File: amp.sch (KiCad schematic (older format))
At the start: 27 parts

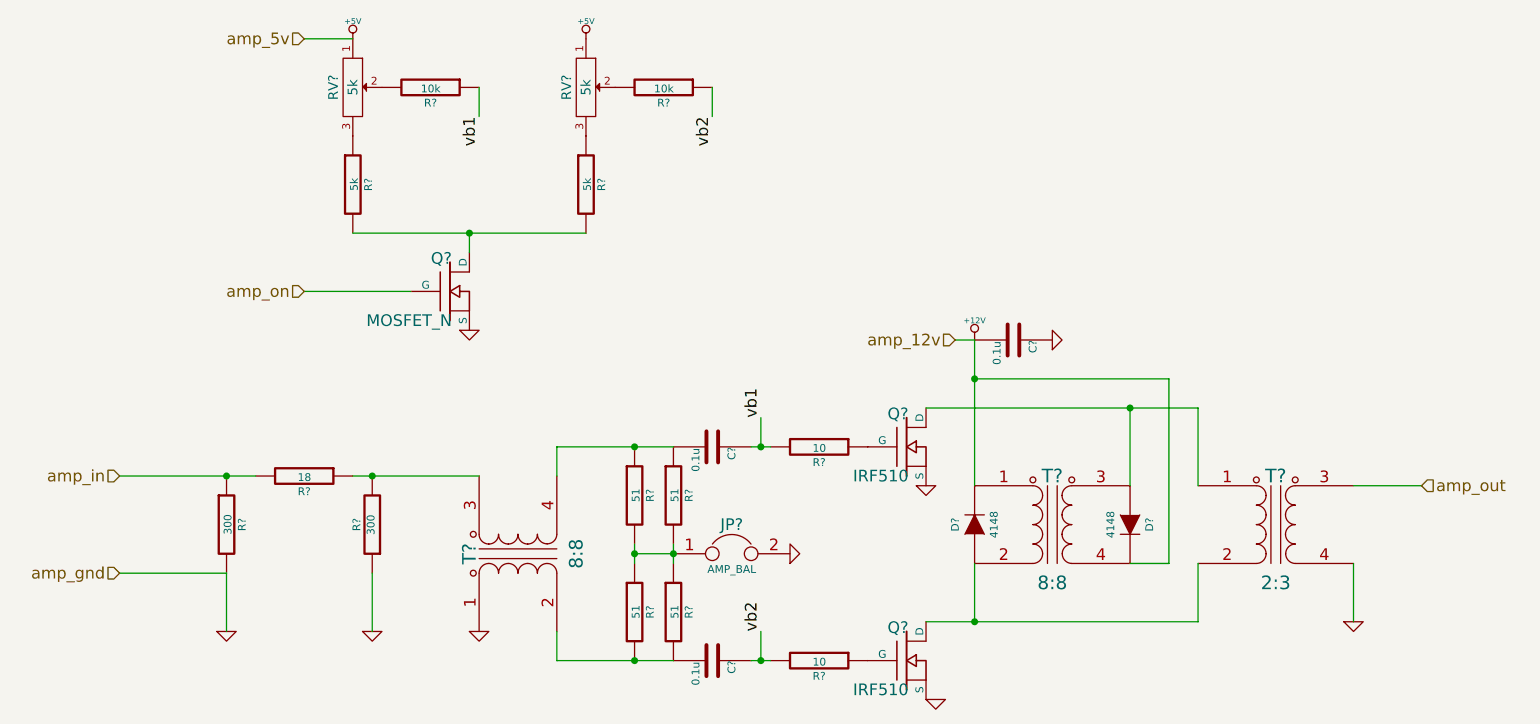
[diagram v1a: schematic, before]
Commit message: Annotated all schematics
- Added more caps to power supply
- Decided on power supply fuse part
- Changed 1n5711 SWR caps to BAT62
- Decided on MMBF170 for amp bias switch
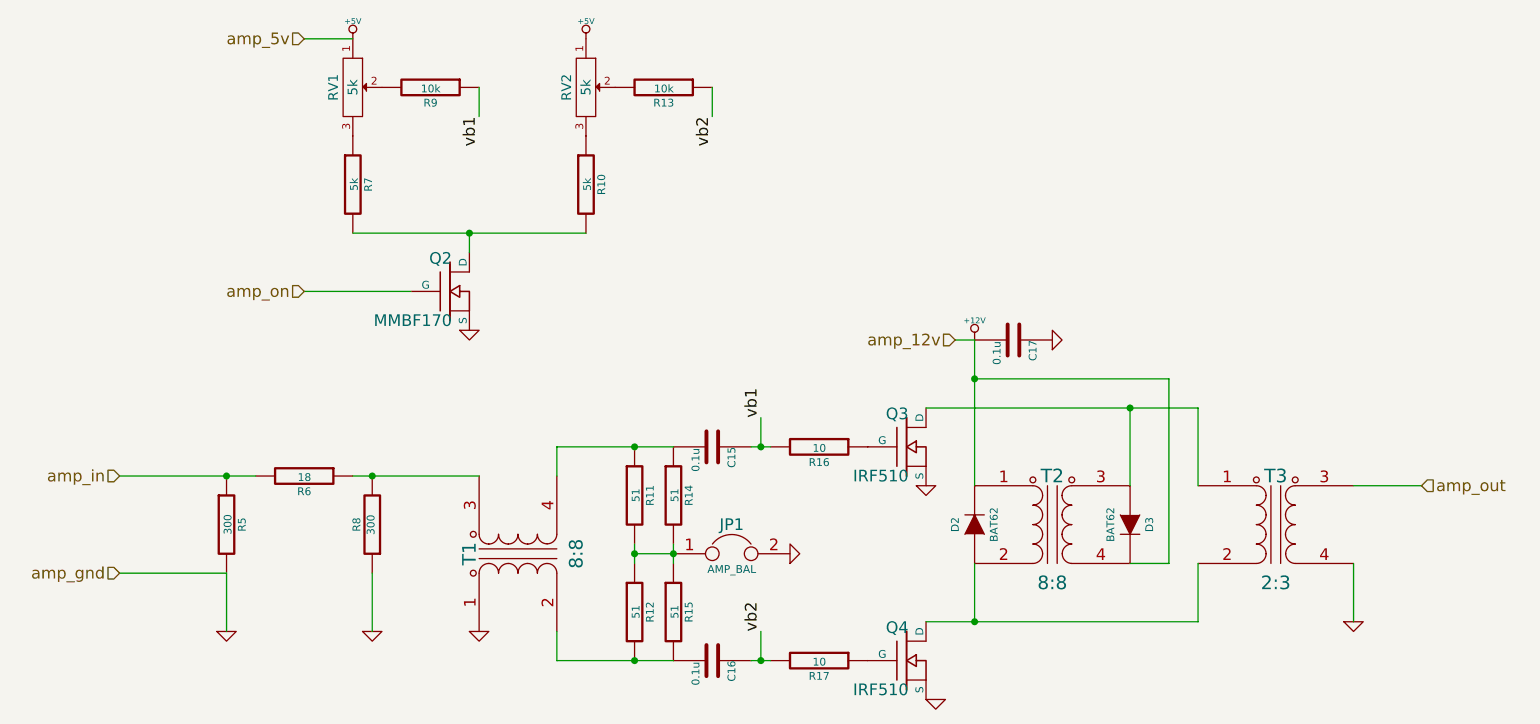
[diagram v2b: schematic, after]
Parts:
- D2, D3: renamed from D?; value 4148 -> BAT62
- Q2: renamed from Q?; value MOSFET_N -> MMBF170
- gave numbers to parts that had none: 24
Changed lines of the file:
@@
 $EndDescr
 $Comp
-L TRANSFO-dots T?
+L TRANSFO-dots T2
 U 1 1 5470F390
 P 7750 4700
-F 0 "T?" H 7750 4950 70  0000 C CNN
+F 0 "T2" H 7750 4950 70  0000 C CNN
 F 1 "8:8" H 7750 4400 70  0000 C CNN
 F 2 "" H 7750 4700 60  0000 C CNN
@@
 $EndComp
 $Comp
-L TRANSFO-dots T?
+L TRANSFO-dots T3
 U 1 1 5470F3A2
 P 8900 4700
-F 0 "T?" H 8900 4950 70  0000 C CNN
+F 0 "T3" H 8900 4950 70  0000 C CNN
 F 1 "2:3" H 8900 4400 70  0000 C CNN
 F 2 "" H 8900 4700 60  0000 C CNN
@@
 $EndComp
 $Comp
-L TRANSFO-dots T?
+L TRANSFO-dots T1
 U 1 1 5470F3AD
 P 5000 4850
-F 0 "T?" H 5000 5100 70  0000 C CNN
+F 0 "T1" H 5000 5100 70  0000 C CNN
 F 1 "8:8" H 5000 4550 70  0000 C CNN
 F 2 "" H 5000 4850 60  0000 C CNN
@@
 $EndComp
 $Comp
-L MOSFET_N Q?
+L MOSFET_N Q3
 U 1 1 5470F3BA
 P 7000 4300
-F 0 "Q?" H 7010 4470 60  0000 R CNN
+F 0 "Q3" H 7010 4470 60  0000 R CNN
 F 1 "IRF510" H 7010 4150 60  0000 R CNN
 F 2 "" H 7000 4300 60  0000 C CNN
@@
 $EndComp
 $Comp
-L MOSFET_N Q?
+L MOSFET_N Q4
 U 1 1 5470F3CC
 P 7000 5400
-F 0 "Q?" H 7010 5570 60  0000 R CNN
+F 0 "Q4" H 7010 5570 60  0000 R CNN
 F 1 "IRF510" H 7010 5250 60  0000 R CNN
 F 2 "" H 7000 5400 60  0000 C CNN
@@
 $EndComp
 $Comp
-L R R?
+L R R5
 U 1 1 5470F3E3
 P 3500 4700
-F 0 "R?" V 3580 4700 40  0000 C CNN
+F 0 "R5" V 3580 4700 40  0000 C CNN
 F 1 "300" V 3507 4701 40  0000 C CNN
 F 2 "" V 3430 4700 30  0000 C CNN
@@
 $EndComp
 $Comp
-L R R?
+L R R6
 U 1 1 5470F3F5
 P 3900 4450
-F 0 "R?" V 3980 4450 40  0000 C CNN
+F 0 "R6" V 3980 4450 40  0000 C CNN
 F 1 "18" V 3907 4451 40  0000 C CNN
 F 2 "" V 3830 4450 30  0000 C CNN
@@
 $EndComp
 $Comp
-L R R?
+L R R8
 U 1 1 5470F400
 P 4250 4700
-F 0 "R?" V 4330 4700 40  0000 C CNN
+F 0 "R8" V 4330 4700 40  0000 C CNN
 F 1 "300" V 4257 4701 40  0000 C CNN
 F 2 "" V 4180 4700 30  0000 C CNN
@@
 $EndComp
 $Comp
-L R R?
+L R R11
 U 1 1 5470F415
 P 5600 4550
-F 0 "R?" V 5680 4550 40  0000 C CNN
+F 0 "R11" V 5680 4550 40  0000 C CNN
 F 1 "51" V 5607 4551 40  0000 C CNN
 F 2 "" V 5530 4550 30  0000 C CNN
@@
 $EndComp
 $Comp
-L R R?
+L R R14
 U 1 1 5470F420
 P 5800 4550
-F 0 "R?" V 5880 4550 40  0000 C CNN
+F 0 "R14" V 5880 4550 40  0000 C CNN
 F 1 "51" V 5807 4551 40  0000 C CNN
 F 2 "" V 5730 4550 30  0000 C CNN
@@
 $EndComp
 $Comp
-L R R?
+L R R12
 U 1 1 5470F42B
 P 5600 5150
-F 0 "R?" V 5680 5150 40  0000 C CNN
+F 0 "R12" V 5680 5150 40  0000 C CNN
 F 1 "51" V 5607 5151 40  0000 C CNN
 F 2 "" V 5530 5150 30  0000 C CNN
@@
 $EndComp
 $Comp
-L R R?
+L R R15
 U 1 1 5470F436
 P 5800 5150
-F 0 "R?" V 5880 5150 40  0000 C CNN
+F 0 "R15" V 5880 5150 40  0000 C CNN
 F 1 "51" V 5807 5151 40  0000 C CNN
 F 2 "" V 5730 5150 30  0000 C CNN
@@
 $EndComp
 $Comp
-L C C?
+L C C15
 U 1 1 5470F443
 P 6000 4300
-F 0 "C?" H 6000 4400 40  0000 L CNN
+F 0 "C15" H 6000 4400 40  0000 L CNN
 F 1 "0.1u" H 6006 4215 40  0000 L CNN
 F 2 "" H 6038 4150 30  0000 C CNN
@@
 $EndComp
 $Comp
-L C C?
+L C C16
 U 1 1 5470F455
 P 6000 5400
-F 0 "C?" H 6000 5500 40  0000 L CNN
+F 0 "C16" H 6000 5500 40  0000 L CNN
 F 1 "0.1u" H 6006 5315 40  0000 L CNN
 F 2 "" H 6038 5250 30  0000 C CNN
@@
 $EndComp
 $Comp
-L R R?
+L R R16
 U 1 1 5470F460
 P 6550 4300
-F 0 "R?" V 6630 4300 40  0000 C CNN
+F 0 "R16" V 6630 4300 40  0000 C CNN
 F 1 "10" V 6557 4301 40  0000 C CNN
 F 2 "" V 6480 4300 30  0000 C CNN
@@
 $EndComp
 $Comp
-L R R?
+L R R17
 U 1 1 5470F475
 P 6550 5400
-F 0 "R?" V 6630 5400 40  0000 C CNN
+F 0 "R17" V 6630 5400 40  0000 C CNN
 F 1 "10" V 6557 5401 40  0000 C CNN
 F 2 "" V 6480 5400 30  0000 C CNN
@@
 	2950 4450 3650 4450
 $Comp
-L GND #PWR?
+L GND #PWR44
 U 1 1 5470F4C6
 P 4800 5250
-F 0 "#PWR?" H 4800 5250 30  0001 C CNN
+F 0 "#PWR44" H 4800 5250 30  0001 C CNN
 F 1 "GND" H 4800 5180 30  0001 C CNN
 F 2 "" H 4800 5250 60  0000 C CNN
@@
 $EndComp
 $Comp
-L GND #PWR?
+L GND #PWR42
 U 1 1 5470F4DA
 P 4250 5250
-F 0 "#PWR?" H 4250 5250 30  0001 C CNN
+F 0 "#PWR42" H 4250 5250 30  0001 C CNN
 F 1 "GND" H 4250 5180 30  0001 C CNN
 F 2 "" H 4250 5250 60  0000 C CNN
@@
 $EndComp
 $Comp
-L GND #PWR?
+L GND #PWR40
 U 1 1 5470F4EE
 P 3500 5250
-F 0 "#PWR?" H 3500 5250 30  0001 C CNN
+F 0 "#PWR40" H 3500 5250 30  0001 C CNN
 F 1 "GND" H 3500 5180 30  0001 C CNN
 F 2 "" H 3500 5250 60  0000 C CNN
@@
 Connection ~ 7350 3950
 $Comp
-L GND #PWR?
+L GND #PWR47
 U 1 1 5470F5FC
 P 7100 4500
-F 0 "#PWR?" H 7100 4500 30  0001 C CNN
+F 0 "#PWR47" H 7100 4500 30  0001 C CNN
 F 1 "GND" H 7100 4430 30  0001 C CNN
 F 2 "" H 7100 4500 60  0000 C CNN
@@
 $EndComp
 $Comp
-L GND #PWR?
+L GND #PWR48
 U 1 1 5470F610
 P 7150 5600
-F 0 "#PWR?" H 7150 5600 30  0001 C CNN
+F 0 "#PWR48" H 7150 5600 30  0001 C CNN
 F 1 "GND" H 7150 5530 30  0001 C CNN
 F 2 "" H 7150 5600 60  0000 C CNN
@@
 amp_in
 $Comp
-L GND #PWR?
+L GND #PWR51
 U 1 1 5470F625
 P 9300 5200
-F 0 "#PWR?" H 9300 5200 30  0001 C CNN
+F 0 "#PWR51" H 9300 5200 30  0001 C CNN
 F 1 "GND" H 9300 5130 30  0001 C CNN
 F 2 "" H 9300 5200 60  0000 C CNN
@@
 amp_out
 $Comp
-L POT RV?
+L POT RV1
 U 1 1 5470F7A1
 P 4150 2450
-F 0 "RV?" H 4150 2350 50  0000 C CNN
+F 0 "RV1" H 4150 2350 50  0000 C CNN
 F 1 "5k" H 4150 2450 50  0000 C CNN
 F 2 "" H 4150 2450 60  0000 C CNN
@@
 $EndComp
 $Comp
-L POT RV?
+L POT RV2
 U 1 1 5470F7B3
 P 5350 2450
-F 0 "RV?" H 5350 2350 50  0000 C CNN
+F 0 "RV2" H 5350 2350 50  0000 C CNN
 F 1 "5k" H 5350 2450 50  0000 C CNN
 F 2 "" H 5350 2450 60  0000 C CNN
@@
 $EndComp
 $Comp
-L R R?
+L R R7
 U 1 1 5470F7C0
 P 4150 2950
-F 0 "R?" V 4230 2950 40  0000 C CNN
+F 0 "R7" V 4230 2950 40  0000 C CNN
 F 1 "5k" V 4157 2951 40  0000 C CNN
 F 2 "" V 4080 2950 30  0000 C CNN
@@
 $EndComp
 $Comp
-L R R?
+L R R10
 U 1 1 5470F7D4
 P 5350 2950
-F 0 "R?" V 5430 2950 40  0000 C CNN
+F 0 "R10" V 5430 2950 40  0000 C CNN
 F 1 "5k" V 5357 2951 40  0000 C CNN
 F 2 "" V 5280 2950 30  0000 C CNN
@@
 $EndComp
 $Comp
-L R R?
+L R R9
 U 1 1 5470F7FC
 P 4550 2450
-F 0 "R?" V 4630 2450 40  0000 C CNN
+F 0 "R9" V 4630 2450 40  0000 C CNN
 F 1 "10k" V 4557 2451 40  0000 C CNN
 F 2 "" V 4480 2450 30  0000 C CNN
@@
 $EndComp
 $Comp
-L R R?
+L R R13
 U 1 1 5470F80E
 P 5750 2450
-F 0 "R?" V 5830 2450 40  0000 C CNN
+F 0 "R13" V 5830 2450 40  0000 C CNN
 F 1 "10k" V 5757 2451 40  0000 C CNN
 F 2 "" V 5680 2450 30  0000 C CNN
@@
 $EndComp
 $Comp
-L +5V #PWR?
+L +5V #PWR41
 U 1 1 5470F81B
 P 4150 2200
-F 0 "#PWR?" H 4150 2290 20  0001 C CNN
+F 0 "#PWR41" H 4150 2290 20  0001 C CNN
 F 1 "+5V" H 4150 2290 30  0000 C CNN
 F 2 "" H 4150 2200 60  0000 C CNN
@@
 $EndComp
 $Comp
-L GND #PWR?
+L GND #PWR43
 U 1 1 5470F84C
 P 4750 3700
-F 0 "#PWR?" H 4750 3700 30  0001 C CNN
+F 0 "#PWR43" H 4750 3700 30  0001 C CNN
 F 1 "GND" H 4750 3630 30  0001 C CNN
 F 2 "" H 4750 3700 60  0000 C CNN
@@
 vb2
 $Comp
-L +12V #PWR?
+L +12V #PWR49
 U 1 1 5470F9E0
 P 7350 3750
-F 0 "#PWR?" H 7350 3700 20  0001 C CNN
+F 0 "#PWR49" H 7350 3700 20  0001 C CNN
 F 1 "+12V" H 7350 3850 30  0000 C CNN
 F 2 "" H 7350 3750 60  0000 C CNN
@@
 $EndComp
 $Comp
-L C C?
+L C C17
 U 1 1 5470F9F4
 P 7550 3750
-F 0 "C?" H 7550 3850 40  0000 L CNN
+F 0 "C17" H 7550 3850 40  0000 L CNN
 F 1 "0.1u" H 7556 3665 40  0000 L CNN
 F 2 "" H 7588 3600 30  0000 C CNN
@@
 $EndComp
 $Comp
-L GND #PWR?
+L GND #PWR50
 U 1 1 5470FA0D
 P 7750 3750
-F 0 "#PWR?" H 7750 3750 30  0001 C CNN
+F 0 "#PWR50" H 7750 3750 30  0001 C CNN
 F 1 "GND" H 7750 3680 30  0001 C CNN
 F 2 "" H 7750 3750 60  0000 C CNN
@@
 $EndComp
 $Comp
-L DIODE D?
+L DIODE D2
 U 1 1 5470FB6F
 P 7350 4700
-F 0 "D?" H 7350 4800 40  0000 C CNN
-F 1 "4148" H 7350 4600 40  0000 C CNN
+F 0 "D2" H 7350 4800 40  0000 C CNN
+F 1 "BAT62" H 7350 4600 40  0000 C CNN
 F 2 "" H 7350 4700 60  0000 C CNN
 F 3 "" H 7350 4700 60  0000 C CNN
@@
 $EndComp
 $Comp
-L DIODE D?
+L DIODE D3
 U 1 1 5470FB81
 P 8150 4700
-F 0 "D?" H 8150 4800 40  0000 C CNN
-F 1 "4148" H 8150 4600 40  0000 C CNN
+F 0 "D3" H 8150 4800 40  0000 C CNN
+F 1 "BAT62" H 8150 4600 40  0000 C CNN
 F 2 "" H 8150 4700 60  0000 C CNN
 F 3 "" H 8150 4700 60  0000 C CNN
@@
 $EndComp
 $Comp
-L GND #PWR?
+L GND #PWR46
 U 1 1 5470FB98
 P 6400 4850
-F 0 "#PWR?" H 6400 4850 30  0001 C CNN
+F 0 "#PWR46" H 6400 4850 30  0001 C CNN
 F 1 "GND" H 6400 4780 30  0001 C CNN
 F 2 "" H 6400 4850 60  0000 C CNN
@@
 Connection ~ 5600 4850
 $Comp
-L JUMPER JP?
+L JUMPER JP1
 U 1 1 5470FBEE
 P 6100 4850
-F 0 "JP?" H 6100 5000 60  0000 C CNN
+F 0 "JP1" H 6100 5000 60  0000 C CNN
 F 1 "AMP_BAL" H 6100 4770 40  0000 C CNN
 F 2 "" H 6100 4850 60  0000 C CNN
@@
 $EndComp
 $Comp
-L MOSFET_N Q?
+L MOSFET_N Q2
 U 1 1 5470FC2F
 P 4650 3500
-F 0 "Q?" H 4660 3670 60  0000 R CNN
-F 1 "MOSFET_N" H 4660 3350 60  0000 R CNN
+F 0 "Q2" H 4660 3670 60  0000 R CNN
+F 1 "MMBF170" H 4660 3350 60  0000 R CNN
 F 2 "" H 4650 3500 60  0000 C CNN
 F 3 "" H 4650 3500 60  0000 C CNN
@@
 Connection ~ 4750 3200
 $Comp
-L +5V #PWR?
+L +5V #PWR45
 U 1 1 5470FCA2
 P 5350 2200
-F 0 "#PWR?" H 5350 2290 20  0001 C CNN
+F 0 "#PWR45" H 5350 2290 20  0001 C CNN
 F 1 "+5V" H 5350 2290 30  0000 C CNN
 F 2 "" H 5350 2200 60  0000 C CNN

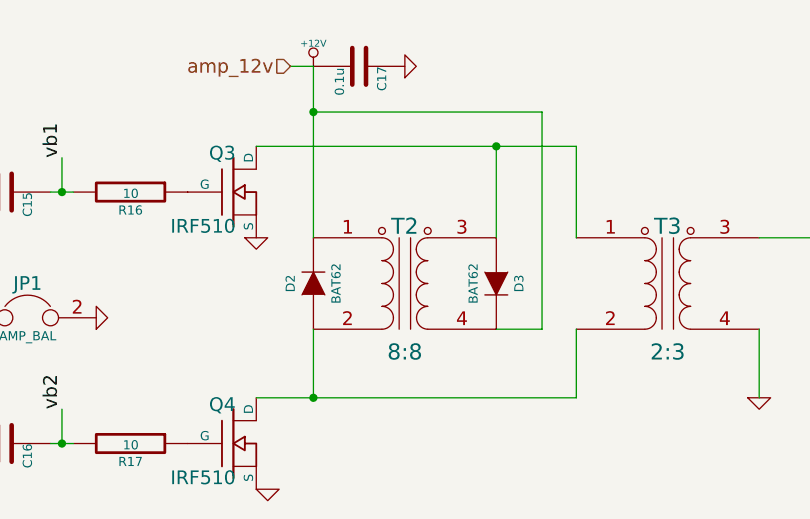
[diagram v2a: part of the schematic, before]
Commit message: Associate more footprints
- Removed flyback diodes from amp
- Changed BAT62 -> SD101 (BAT62 is EOL)
- Changed R and C footprints for hand-soldered versions
- Associated through-hole cap footprints
- Associated regulator footprints
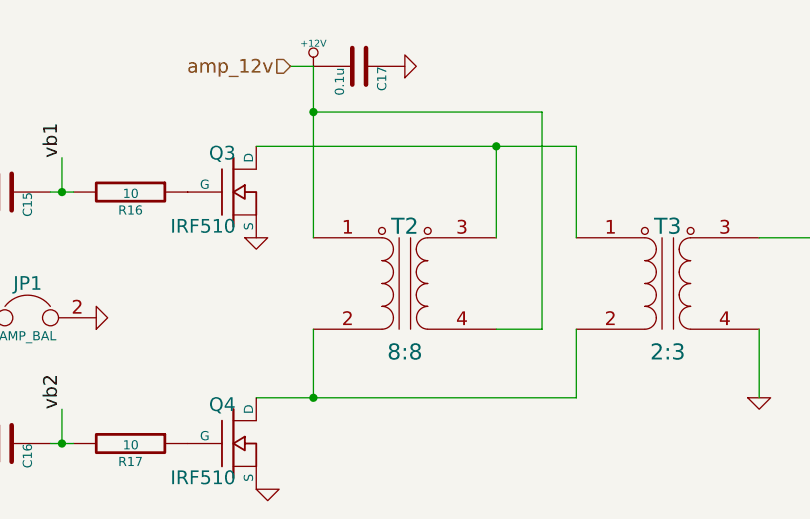
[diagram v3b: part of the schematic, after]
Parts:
- removed D2, D3: BAT62, symbol DIODE
- R10, R13, R16, R17, R7, R9: footprint (none) -> Resistors_SMD:R_1206_HandSoldering
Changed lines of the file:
@@
 LIBS:transformers
 LIBS:qrpamp-cache
-EELAYER 24 0
+EELAYER 25 0
 EELAYER END
 $Descr A4 11693 8268
@@
 F 0 "T2" H 7750 4950 70  0000 C CNN
 F 1 "8:8" H 7750 4400 70  0000 C CNN
-F 2 "" H 7750 4700 60  0000 C CNN
+F 2 "" H 7750 4700 60  0001 C CNN
 F 3 "" H 7750 4700 60  0000 C CNN
 	1    7750 4700
@@
 F 0 "T3" H 8900 4950 70  0000 C CNN
 F 1 "2:3" H 8900 4400 70  0000 C CNN
-F 2 "" H 8900 4700 60  0000 C CNN
+F 2 "" H 8900 4700 60  0001 C CNN
 F 3 "" H 8900 4700 60  0000 C CNN
 	1    8900 4700
@@
 F 0 "T1" H 5000 5100 70  0000 C CNN
 F 1 "8:8" H 5000 4550 70  0000 C CNN
-F 2 "" H 5000 4850 60  0000 C CNN
+F 2 "" H 5000 4850 60  0001 C CNN
 F 3 "" H 5000 4850 60  0000 C CNN
 	1    5000 4850
@@
 F 0 "Q3" H 7010 4470 60  0000 R CNN
 F 1 "IRF510" H 7010 4150 60  0000 R CNN
-F 2 "" H 7000 4300 60  0000 C CNN
+F 2 "" H 7000 4300 60  0001 C CNN
 F 3 "" H 7000 4300 60  0000 C CNN
 	1    7000 4300
@@
 F 0 "Q4" H 7010 5570 60  0000 R CNN
 F 1 "IRF510" H 7010 5250 60  0000 R CNN
-F 2 "" H 7000 5400 60  0000 C CNN
+F 2 "" H 7000 5400 60  0001 C CNN
 F 3 "" H 7000 5400 60  0000 C CNN
 	1    7000 5400
@@
 F 0 "R5" V 3580 4700 40  0000 C CNN
 F 1 "300" V 3507 4701 40  0000 C CNN
-F 2 "" V 3430 4700 30  0000 C CNN
+F 2 "" V 3430 4700 30  0001 C CNN
 F 3 "" H 3500 4700 30  0000 C CNN
 	1    3500 4700
@@
 F 0 "R6" V 3980 4450 40  0000 C CNN
 F 1 "18" V 3907 4451 40  0000 C CNN
-F 2 "" V 3830 4450 30  0000 C CNN
+F 2 "" V 3830 4450 30  0001 C CNN
 F 3 "" H 3900 4450 30  0000 C CNN
 	1    3900 4450
@@
 F 0 "R8" V 4330 4700 40  0000 C CNN
 F 1 "300" V 4257 4701 40  0000 C CNN
-F 2 "" V 4180 4700 30  0000 C CNN
+F 2 "" V 4180 4700 30  0001 C CNN
 F 3 "" H 4250 4700 30  0000 C CNN
 	1    4250 4700
@@
 F 0 "R11" V 5680 4550 40  0000 C CNN
 F 1 "51" V 5607 4551 40  0000 C CNN
-F 2 "" V 5530 4550 30  0000 C CNN
+F 2 "" V 5530 4550 30  0001 C CNN
 F 3 "" H 5600 4550 30  0000 C CNN
 	1    5600 4550
@@
 F 0 "R14" V 5880 4550 40  0000 C CNN
 F 1 "51" V 5807 4551 40  0000 C CNN
-F 2 "" V 5730 4550 30  0000 C CNN
+F 2 "" V 5730 4550 30  0001 C CNN
 F 3 "" H 5800 4550 30  0000 C CNN
 	1    5800 4550
@@
 F 0 "R12" V 5680 5150 40  0000 C CNN
 F 1 "51" V 5607 5151 40  0000 C CNN
-F 2 "" V 5530 5150 30  0000 C CNN
+F 2 "" V 5530 5150 30  0001 C CNN
 F 3 "" H 5600 5150 30  0000 C CNN
 	1    5600 5150
@@
 F 0 "R15" V 5880 5150 40  0000 C CNN
 F 1 "51" V 5807 5151 40  0000 C CNN
-F 2 "" V 5730 5150 30  0000 C CNN
+F 2 "" V 5730 5150 30  0001 C CNN
 F 3 "" H 5800 5150 30  0000 C CNN
 	1    5800 5150
@@
 F 0 "C15" H 6000 4400 40  0000 L CNN
 F 1 "0.1u" H 6006 4215 40  0000 L CNN
-F 2 "" H 6038 4150 30  0000 C CNN
+F 2 "" H 6038 4150 30  0001 C CNN
 F 3 "" H 6000 4300 60  0000 C CNN
 	1    6000 4300
@@
 F 0 "C16" H 6000 5500 40  0000 L CNN
 F 1 "0.1u" H 6006 5315 40  0000 L CNN
-F 2 "" H 6038 5250 30  0000 C CNN
+F 2 "" H 6038 5250 30  0001 C CNN
 F 3 "" H 6000 5400 60  0000 C CNN
 	1    6000 5400
@@
 F 0 "R16" V 6630 4300 40  0000 C CNN
 F 1 "10" V 6557 4301 40  0000 C CNN
-F 2 "" V 6480 4300 30  0000 C CNN
+F 2 "Resistors_SMD:R_1206_HandSoldering" V 6480 4300 30  0001 C CNN
 F 3 "" H 6550 4300 30  0000 C CNN
 	1    6550 4300
@@
 F 0 "R17" V 6630 5400 40  0000 C CNN
 F 1 "10" V 6557 5401 40  0000 C CNN
-F 2 "" V 6480 5400 30  0000 C CNN
+F 2 "Resistors_SMD:R_1206_HandSoldering" V 6480 5400 30  0001 C CNN
 F 3 "" H 6550 5400 30  0000 C CNN
 	1    6550 5400
@@
 F 0 "RV1" H 4150 2350 50  0000 C CNN
 F 1 "5k" H 4150 2450 50  0000 C CNN
-F 2 "" H 4150 2450 60  0000 C CNN
+F 2 "" H 4150 2450 60  0001 C CNN
 F 3 "" H 4150 2450 60  0000 C CNN
 	1    4150 2450
@@
 F 0 "RV2" H 5350 2350 50  0000 C CNN
 F 1 "5k" H 5350 2450 50  0000 C CNN
-F 2 "" H 5350 2450 60  0000 C CNN
+F 2 "" H 5350 2450 60  0001 C CNN
 F 3 "" H 5350 2450 60  0000 C CNN
 	1    5350 2450
@@
 F 0 "R7" V 4230 2950 40  0000 C CNN
 F 1 "5k" V 4157 2951 40  0000 C CNN
-F 2 "" V 4080 2950 30  0000 C CNN
+F 2 "Resistors_SMD:R_1206_HandSoldering" V 4080 2950 30  0001 C CNN
 F 3 "" H 4150 2950 30  0000 C CNN
 	1    4150 2950
@@
 F 0 "R10" V 5430 2950 40  0000 C CNN
 F 1 "5k" V 5357 2951 40  0000 C CNN
-F 2 "" V 5280 2950 30  0000 C CNN
+F 2 "Resistors_SMD:R_1206_HandSoldering" V 5280 2950 30  0001 C CNN
 F 3 "" H 5350 2950 30  0000 C CNN
 	1    5350 2950
@@
 F 0 "R9" V 4630 2450 40  0000 C CNN
 F 1 "10k" V 4557 2451 40  0000 C CNN
-F 2 "" V 4480 2450 30  0000 C CNN
+F 2 "Resistors_SMD:R_1206_HandSoldering" V 4480 2450 30  0001 C CNN
 F 3 "" H 4550 2450 30  0000 C CNN
 	1    4550 2450
@@
 F 0 "R13" V 5830 2450 40  0000 C CNN
 F 1 "10k" V 5757 2451 40  0000 C CNN
-F 2 "" V 5680 2450 30  0000 C CNN
+F 2 "Resistors_SMD:R_1206_HandSoldering" V 5680 2450 30  0001 C CNN
 F 3 "" H 5750 2450 30  0000 C CNN
 	1    5750 2450
@@
 F 0 "C17" H 7550 3850 40  0000 L CNN
 F 1 "0.1u" H 7556 3665 40  0000 L CNN
-F 2 "" H 7588 3600 30  0000 C CNN
+F 2 "" H 7588 3600 30  0001 C CNN
 F 3 "" H 7550 3750 60  0000 C CNN
 	1    7550 3750
@@
 $EndComp
 $Comp
-L DIODE D2
-U 1 1 5470FB6F
-P 7350 4700
-F 0 "D2" H 7350 4800 40  0000 C CNN
-F 1 "BAT62" H 7350 4600 40  0000 C CNN
-F 2 "" H 7350 4700 60  0000 C CNN
-F 3 "" H 7350 4700 60  0000 C CNN
-	1    7350 4700
-	0    -1   -1   0
-$EndComp
-$Comp
-L DIODE D3
-U 1 1 5470FB81
-P 8150 4700
-F 0 "D3" H 8150 4800 40  0000 C CNN
-F 1 "BAT62" H 8150 4600 40  0000 C CNN
-F 2 "" H 8150 4700 60  0000 C CNN
-F 3 "" H 8150 4700 60  0000 C CNN
-	1    8150 4700
-	0    1    1    0
-$EndComp
-$Comp
 L GND #PWR46
 U 1 1 5470FB98
@@
 F 0 "JP1" H 6100 5000 60  0000 C CNN
 F 1 "AMP_BAL" H 6100 4770 40  0000 C CNN
-F 2 "" H 6100 4850 60  0000 C CNN
+F 2 "" H 6100 4850 60  0001 C CNN
 F 3 "" H 6100 4850 60  0000 C CNN
 	1    6100 4850
@@
 F 0 "Q2" H 4660 3670 60  0000 R CNN
 F 1 "MMBF170" H 4660 3350 60  0000 R CNN
-F 2 "" H 4650 3500 60  0000 C CNN
+F 2 "" H 4650 3500 60  0001 C CNN
 F 3 "" H 4650 3500 60  0000 C CNN
 	1    4650 3500
